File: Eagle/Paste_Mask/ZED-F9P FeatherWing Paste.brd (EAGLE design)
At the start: 50.8 x 22.9 mm, 26 parts, among them U1 ZED-F9P_ZED-F9P, U2 SPX3819-3.3

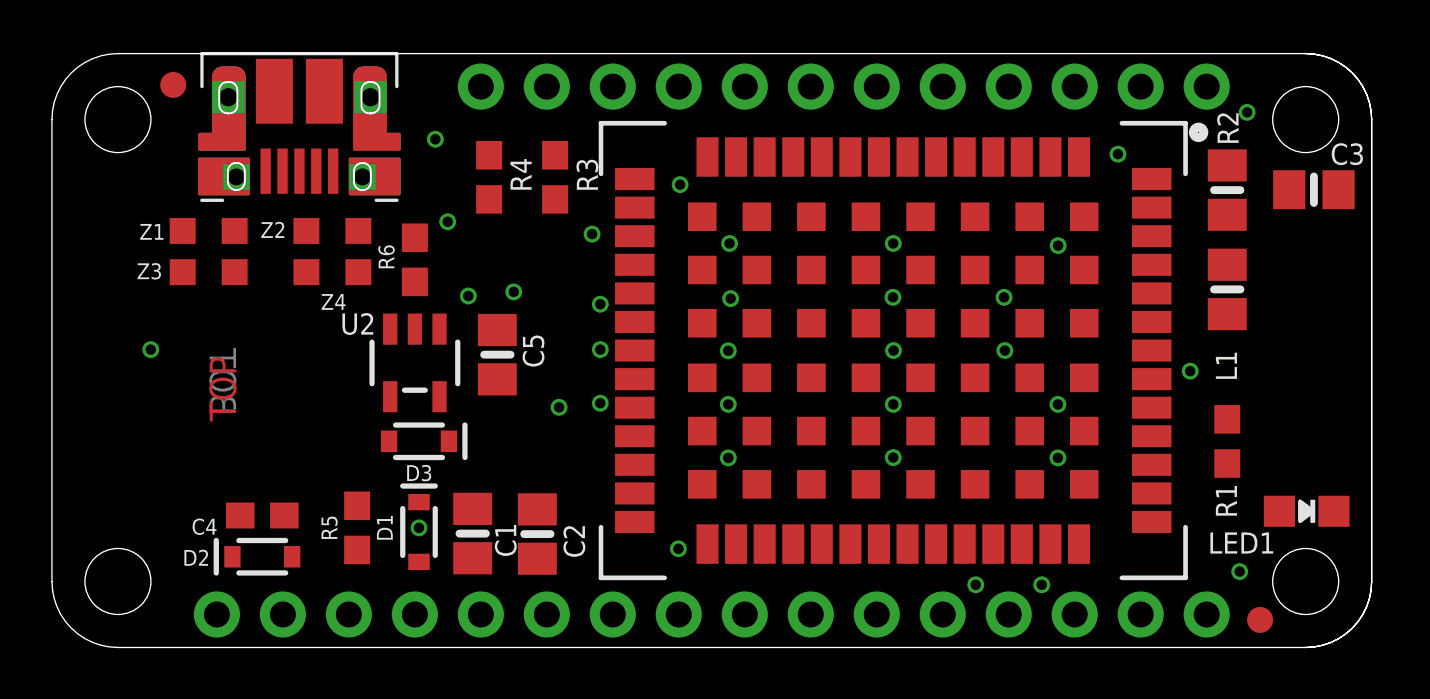
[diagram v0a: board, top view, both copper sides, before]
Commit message: Updated the power circuit
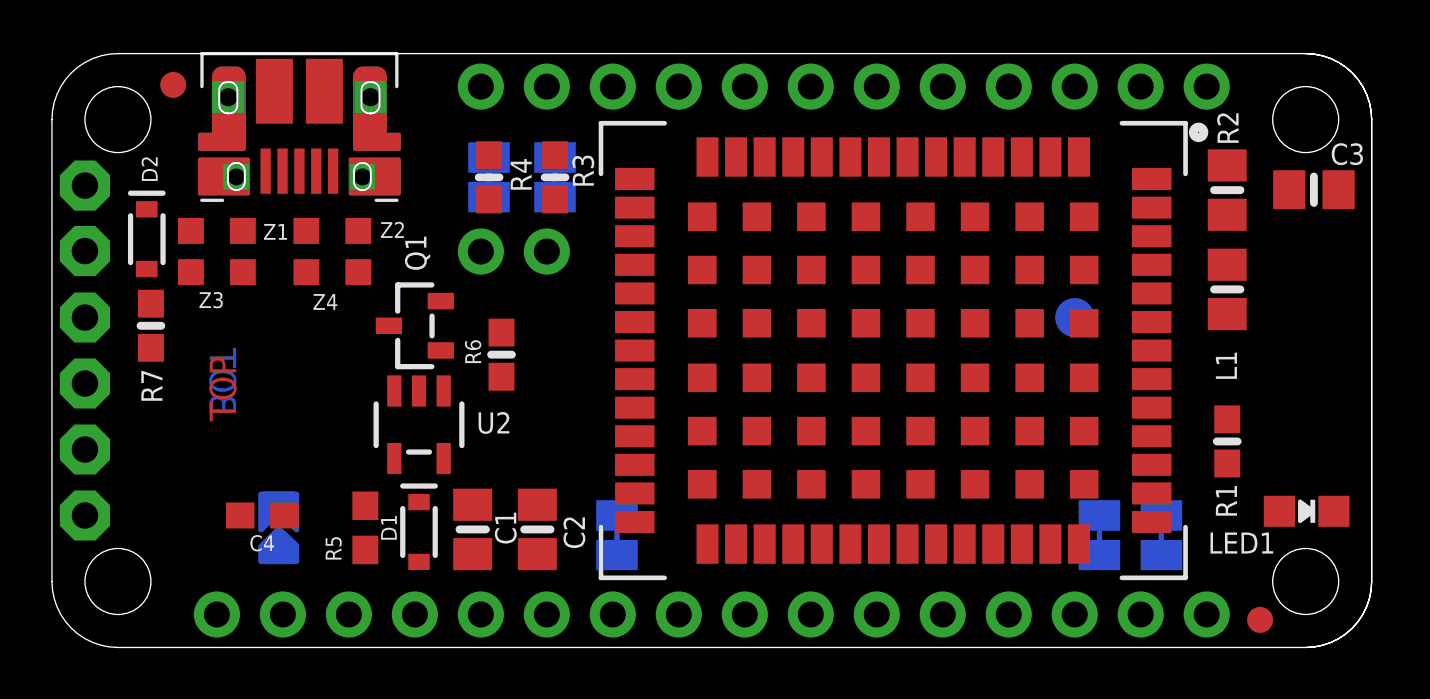
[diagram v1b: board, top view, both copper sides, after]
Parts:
- removed C5: 10µF, microbuilder:0805-NO
- removed D3: 0.5A/40V/420mV, SparkFun-DiscreteSemi:SOD-323
- added 3.3V: (no value), microbuilder:SOLDERJUMPER_ARROW_NOPASTE
- added 3V3, CTS, GND, RTS, RX2, TX2: (no value), adafruit:1X01
- added INT, RX, SCL, SDA, TX: (no value), microbuilder:SOLDERJUMPER_CLOSEDWIRE
- added JP5: (no value), microbuilder:1X02_ROUND
- added Q1: DMG2305, microbuilder:SOT23-R
- added R7: 100K, microbuilder:0603-NO
- added TP1: (no value), microbuilder:TESTPOINT_ROUND_1.5MM
- moved D2 13.0 mm to (3.65, 15.7), turned to 270 degrees
- moved R6 4.94 mm to (17.3, 11.3)
- moved U2 2.39 mm to (14.1, 8.57)
- moved Z1 0.32 mm to (6.35, 16.0)
- moved Z3 0.32 mm to (6.35, 14.4)
- moved R5 0.32 mm to (12.1, 4.60)
- moved C2 0.18 mm to (18.7, 4.54)
- moved C1 0.16 mm to (16.2, 4.54)
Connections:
- removed net N$1: C1.1
- new net VBAT: Q1.3
